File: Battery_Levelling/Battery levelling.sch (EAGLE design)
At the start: 36 parts, among them CON1 MOLEX_5566-2, CON2 SM03B-GHS-TB, CON3 SM03B-GHS-TB, J1 MKDS_5/2-6,352, J2 MKDS_5/2-6,352, J3 MKDS_5/2-6,352, J4 MKDS_5/2-6,352, J5 MKDS_5/2-6,352, U1 TEENSY_3.1_BASIC_2, U3 TCAN1042HVDR

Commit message: Added channel, changed CAN transceiver, used NMOS
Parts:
- removed T2: (no value), transistor-neu-to92:-NPN-SOT223
- removed U$2: LM5050-2, AlbertaSat:LM5050-2
- removed U$7: PMOS-SO8, AlbertaSat:PMOS-SO8
- added C6: 10u, rcl:C-EUC0805
- added C7: 1.5uF, adafruit:C-USC0805
- added C8: 10uF, adafruit:C-USC1206
- added D1: (no value), diode:DIODE-DO-214AC
- added J6: MKDS_5/2-6,352, Moira:MKDS_5/2-6,352
- added Q4: NMOS-TO252, AlbertaSat:NMOS-TO252
- added Q5: DMN2011UTS, Lydia:DMN2011UTS
- added R11: 100k, adafruit:R-US_R1206
- added U5: LM5050-2, AlbertaSat:LM5050-2
- added U6: IR2301S, Lydia:IR2301S
- added U7: MCP2562-E/SN, Lydia:MCP2562-E/SN
- C4: value 10u -> 0.01uF; device rcl:C-EUC0805 -> adafruit:C-USC0805
- R10: value 100k -> 1k; device adafruit:R-US_R1206 -> rcl:R-US_R0805
- R4: value 5k -> 5.1
- U3: value TCAN1042HVDR -> LM5050-2; device ARVP:TCAN1042HVDR -> AlbertaSat:LM5050-2
- renumbered U$1 to U2, U$3 to U4, U$4 to Q2, U$5 to Q1, U$6 to Q3
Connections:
- removed net VBATT0: R4.1, T2.C, U$7.G
- removed net VOUT1: J5.KL, U$2.OUT, U$7.D, U2.OUT, U4.OUT
- new net GATE4: Q4.G, U5.GATE
- new net GATE5: R10.1, U6.HO
- new net IO6: R11.1, U1.10/TX2/PWM, U5.NFGD
- new net N$4: C7.2, U6.VS
- new net N$5: C7.1, D1.C, U6.VB
- new net N$6: U7.VIO
- new net N$7: Q5.G, R10.2
- new net VBATT4: J6.KL1, Q4.S
- net +3V3: now also C6.1; no longer C4.1, U3.VIO
- net +5V: now also R11.2
- net CANH1: now also U7.CANH; no longer U3.CANH
- net CANL1: now also U7.CANL; no longer U3.CANL
- net CAN_RX1: now also U7.RXD; no longer U3.RXD
- net CAN_TX2: now also U7.TXD; no longer U3.TXD
- net GATE2: now also U3.GATE; no longer U$2.GATE
- net GND: now also C6.2, C8.2, J6.KL, U5.GND, U6.GND, U6.LIN, U7.VSS; no longer T2.E, U$2.GND
- net IO1: now also U6.HIN; no longer R10.2
- net IO2: now also U3.OFF, U5.OFF; no longer U$2.OFF
- net IO3: now also U3.NFGD; no longer U$2.NFGD
- net N$1: now also C8.1, Q5.D, R4.1, U6.VCC; no longer R4.2, U$7.S
- net N$3: now also D1.A, R4.2; no longer R10.1, T2.B
- net STB1: now also U7.STBY; no longer U3.STB
- net VBATT2: now also U3.IN; no longer U$2.IN
- net VBATT3: now also C4.1, U5.IN
- net VIN: now also U7.VDD; no longer U3.VCC
- net VOUT: now also J5.KL, Q4.D, Q5.S, U2.OUT, U3.OUT, U4.OUT, U5.OUT
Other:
- note added: "A high side NMOS switch controls the original electronics battery (BATT0) using a high side gate driver with a bootstap circuit. When the GPIO pin is low, the NMOS is not conducting. When the GPIO pin is high, the gate driver will turn on and drive the NMOS with battery voltage+bootstrap voltage."
- note added: "The bootstrap circuit uses a capacitor C7 to store charge on a low cycle. Stored charge will be used to bias VCC to increase the voltage at HO during high cycles in order to increase the voltage between the NMOS gate and source. C7 will slowly discharge during a high cycle, so the capcitance is chosen to be 10 times greater than the gate capacitance of the NMOS to prolong the discharge. The bypas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"
- note removed: "A PMOS controls the original electronics battery (BATT0) using a BJT and a GPIO pin. When the GPIO pin is low, the PMOS is not conducting. When the GPIO pin is high, current will flow through the transistor and the gate and source of the PMOS will have a voltage difference (Vg < Vs) causing the PMOSto conduct."
- note removed: "The BJT base current is designed to be 23uA. The BJT has a current gain of 25 at the design condition, giving a collector current of 0.58 mA. When the BJT is on, Vgs will be around -2.9V. The PMOS chosen has a Vth of -1.4V and will be turned on as well."
- moved on the sheet: C4, C5, CON2-1, CON2-2, CON2-3, CON2-TABS, CON3-1, CON3-2, CON3-3, CON3-TABS, R1, R10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

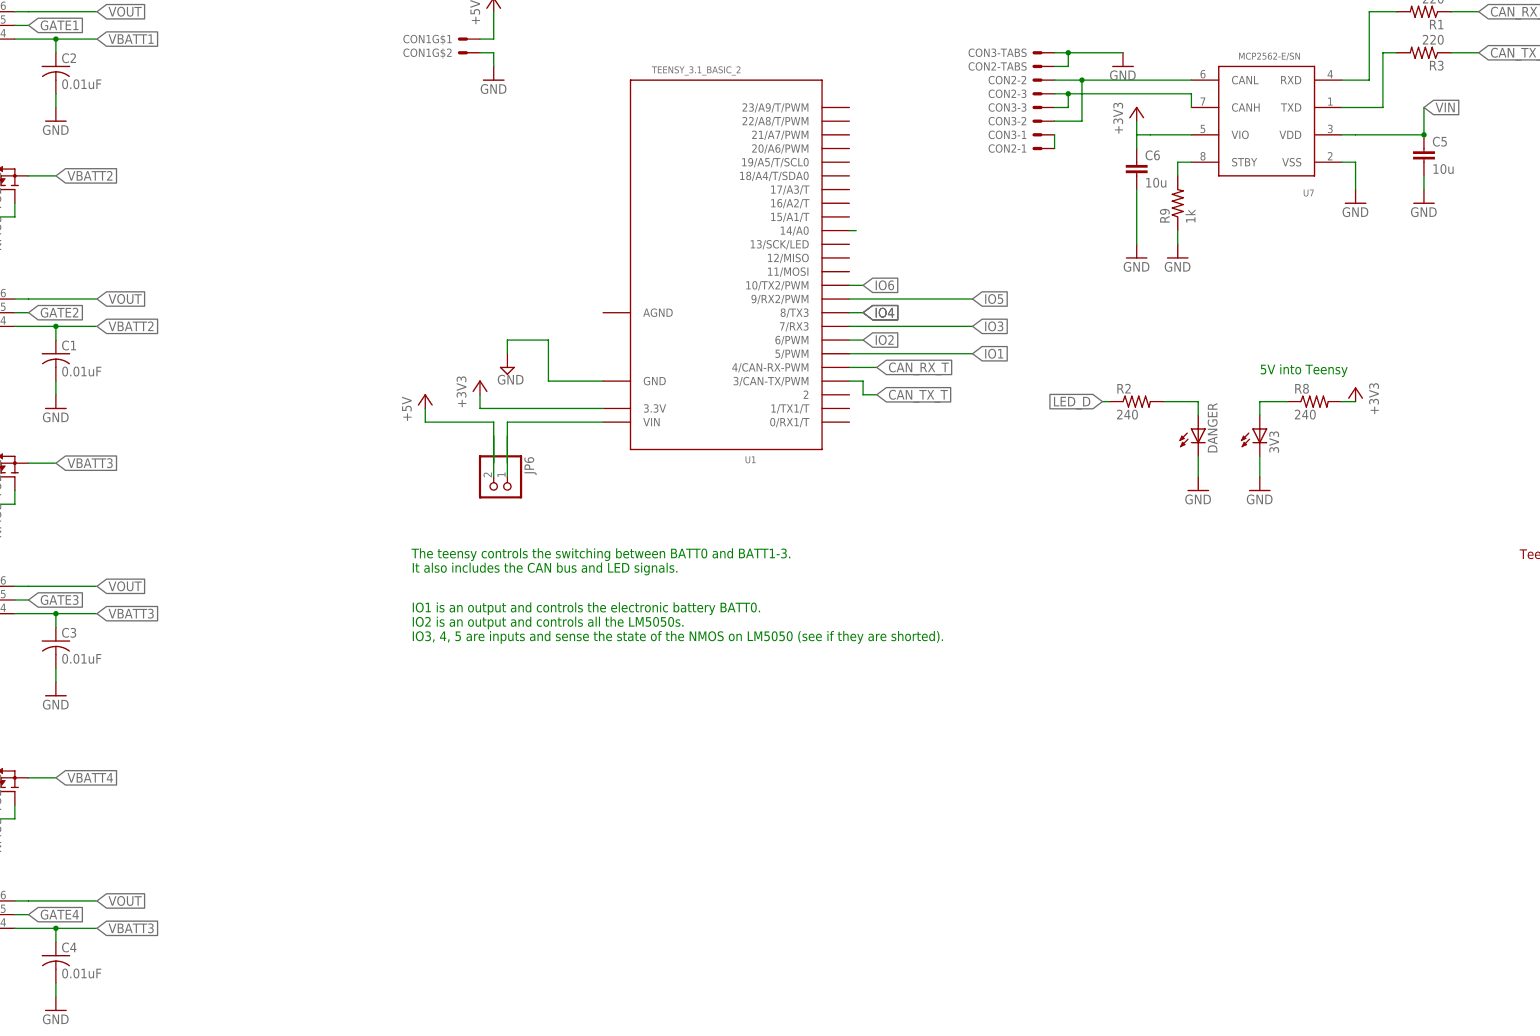
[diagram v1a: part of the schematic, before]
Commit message: Added PCB board file for battery levelling board
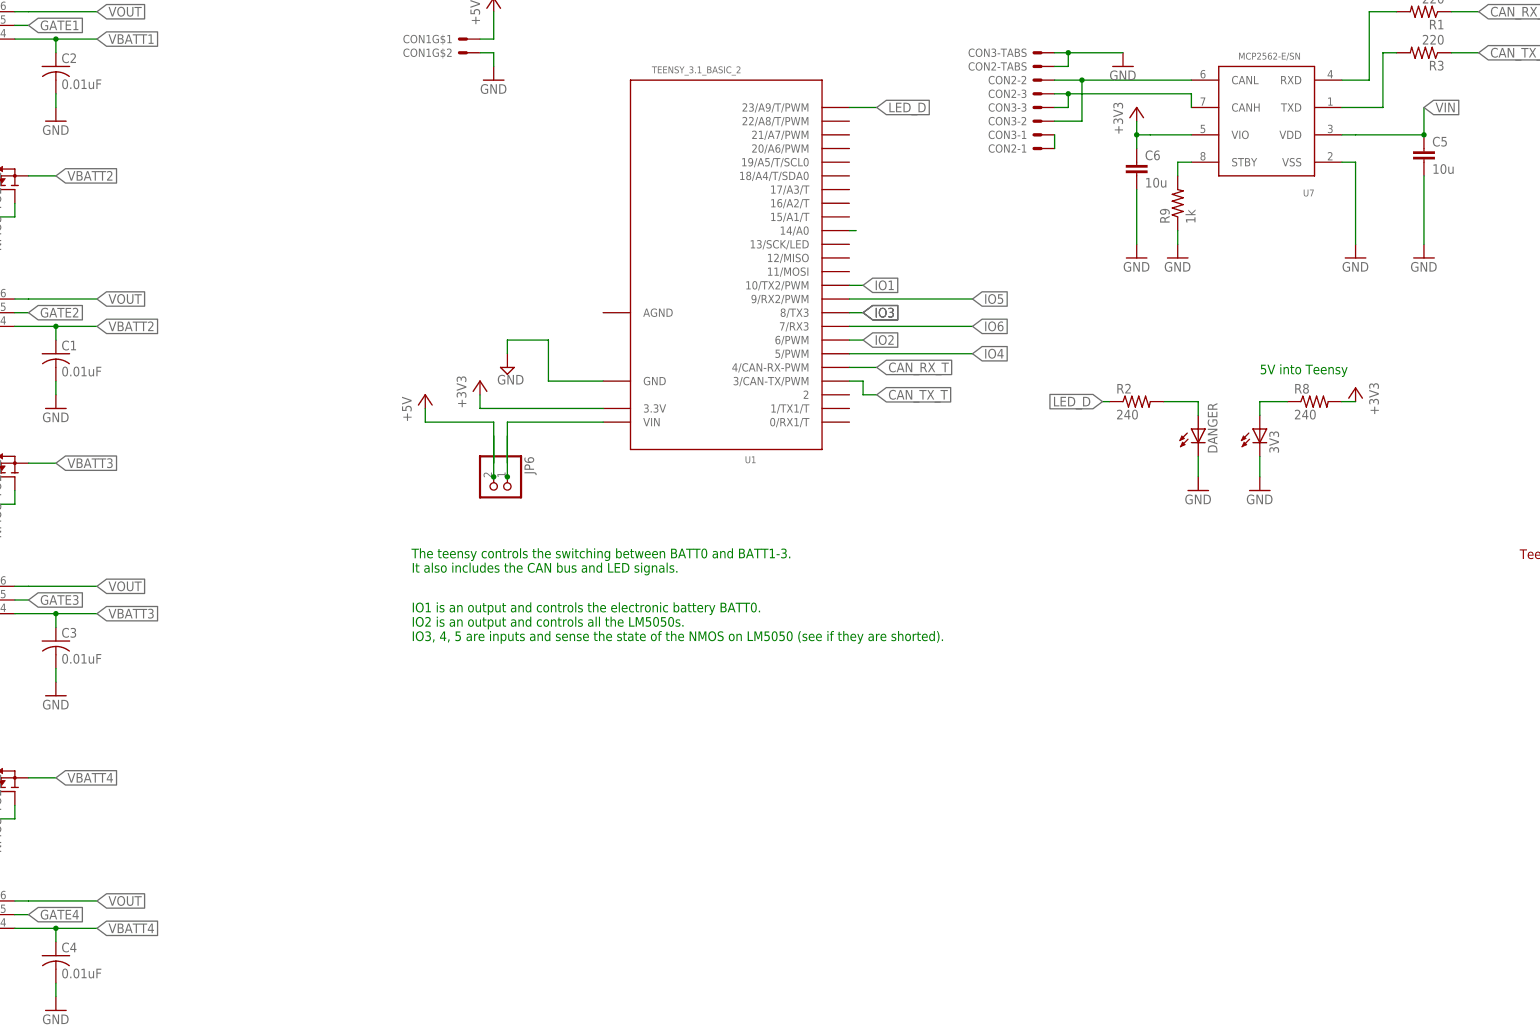
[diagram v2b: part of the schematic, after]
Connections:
- removed net N$6: U7.VIO
- net +3V3: now also U7.VIO
- net IO1: now also U1.10/TX2/PWM; no longer U1.5/PWM
- net IO3: now also U1.8/TX3; no longer U1.7/RX3
- net IO4: now also U1.5/PWM; no longer U1.8/TX3
- net IO6: now also U1.7/RX3; no longer U1.10/TX2/PWM
- net LED_D: now also U1.23/A9/T/PWM
- net VBATT3: no longer C4.1, U5.IN
- net VBATT4: now also C4.1, U5.IN
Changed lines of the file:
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@@
 <instance part="P+1" gate="1" x="152.4" y="-7.62"/>
 <instance part="+3V34" gate="G$1" x="284.48" y="45.72"/>
-<instance part="GND6" gate="1" x="325.12" y="27.94"/>
+<instance part="GND6" gate="1" x="325.12" y="17.78"/>
 <instance part="C6" gate="G$1" x="284.48" y="35.56"/>
 <instance part="GND7" gate="1" x="284.48" y="17.78"/>
 <instance part="C5" gate="G$1" x="337.82" y="38.1"/>
-<instance part="GND10" gate="1" x="337.82" y="27.94"/>
+<instance part="GND10" gate="1" x="337.82" y="17.78"/>
 <instance part="R9" gate="G$1" x="292.1" y="27.94" rot="R90"/>
 <instance part="GND11" gate="1" x="292.1" y="17.78"/>
@@
 <net name="IO1" class="0">
 <segment>
-<pinref part="U1" gate="G$1" pin="5/PWM"/>
-<wire x1="231.14" y1="0" x2="254" y2="0" width="0.1524" layer="91"/>
-<label x="254" y="0" size="1.778" layer="95" xref="yes"/>
-</segment>
-<segment>
 <wire x1="-106.68" y1="33.02" x2="-114.3" y2="33.02" width="0.1524" layer="91"/>
 <label x="-114.3" y="33.02" size="1.778" layer="95" rot="R180" xref="yes"/>
 <pinref part="U6" gate="G$1" pin="HIN"/>
+</segment>
+<segment>
+<wire x1="231.14" y1="12.7" x2="233.68" y2="12.7" width="0.1524" layer="91"/>
+<label x="233.68" y="12.7" size="1.778" layer="95" xref="yes"/>
+<pinref part="U1" gate="G$1" pin="10/TX2/PWM"/>
 </segment>
 </net>
@@
 <pinref part="Q3" gate="G$1" pin="S"/>
 </segment>
-<segment>
-<wire x1="76.2" y1="-106.68" x2="83.82" y2="-106.68" width="0.1524" layer="91"/>
-<label x="91.44" y="-106.68" size="1.778" layer="95" xref="yes"/>
-<pinref part="U5" gate="G$1" pin="IN"/>
-<pinref part="C4" gate="G$1" pin="1"/>
-<wire x1="83.82" y1="-106.68" x2="91.44" y2="-106.68" width="0.1524" layer="91"/>
-<wire x1="83.82" y1="-106.68" x2="83.82" y2="-109.22" width="0.1524" layer="91"/>
-<junction x="83.82" y="-106.68"/>
-</segment>
 </net>
 <net name="GATE3" class="0">
@@
 <pinref part="GND6" gate="1" pin="GND"/>
 <wire x1="322.58" y1="35.56" x2="325.12" y2="35.56" width="0.1524" layer="91"/>
-<wire x1="325.12" y1="35.56" x2="325.12" y2="30.48" width="0.1524" layer="91"/>
+<wire x1="325.12" y1="35.56" x2="325.12" y2="20.32" width="0.1524" layer="91"/>
 <pinref part="U7" gate="G$1" pin="VSS"/>
 </segment>
@@
 <pinref part="C5" gate="G$1" pin="2"/>
 <pinref part="GND10" gate="1" pin="GND"/>
-<wire x1="337.82" y1="33.02" x2="337.82" y2="30.48" width="0.1524" layer="91"/>
+<wire x1="337.82" y1="33.02" x2="337.82" y2="20.32" width="0.1524" layer="91"/>
 </segment>
 <segment>
@@
 </segment>
 <segment>
-<pinref part="U1" gate="G$1" pin="8/TX3"/>
-<wire x1="231.14" y1="7.62" x2="233.68" y2="7.62" width="0.1524" layer="91"/>
-<label x="233.68" y="7.62" size="1.778" layer="95" xref="yes"/>
-<label x="233.68" y="7.62" size="1.778" layer="95" xref="yes"/>
+<pinref part="U1" gate="G$1" pin="5/PWM"/>
+<wire x1="231.14" y1="0" x2="254" y2="0" width="0.1524" layer="91"/>
+<label x="254" y="0" size="1.778" layer="95" xref="yes"/>
 </segment>
 </net>
@@
 </segment>
 <segment>
-<pinref part="U1" gate="G$1" pin="7/RX3"/>
-<wire x1="231.14" y1="5.08" x2="254" y2="5.08" width="0.1524" layer="91"/>
-<label x="254" y="5.08" size="1.778" layer="95" xref="yes"/>
+<pinref part="U1" gate="G$1" pin="8/TX3"/>
+<wire x1="231.14" y1="7.62" x2="233.68" y2="7.62" width="0.1524" layer="91"/>
+<label x="233.68" y="7.62" size="1.778" layer="95" xref="yes"/>
+<label x="233.68" y="7.62" size="1.778" layer="95" xref="yes"/>
 </segment>
 </net>
@@
 <pinref part="+3V34" gate="G$1" pin="+3V3"/>
 <pinref part="C6" gate="G$1" pin="1"/>
-<wire x1="284.48" y1="43.18" x2="284.48" y2="38.1" width="0.1524" layer="91"/>
+<wire x1="284.48" y1="43.18" x2="284.48" y2="40.64" width="0.1524" layer="91"/>
+<pinref part="U7" gate="G$1" pin="VIO"/>
+<wire x1="284.48" y1="40.64" x2="284.48" y2="38.1" width="0.1524" layer="91"/>
+<wire x1="294.64" y1="40.64" x2="287.02" y2="40.64" width="0.1524" layer="91"/>
+<wire x1="284.48" y1="40.64" x2="287.02" y2="40.64" width="0.1524" layer="91"/>
+<junction x="284.48" y="40.64"/>
 </segment>
 </net>
@@
 <wire x1="279.4" y1="-8.89" x2="278.13" y2="-8.89" width="0.1524" layer="91"/>
 <label x="278.13" y="-8.89" size="1.778" layer="95" rot="R180" xref="yes"/>
+</segment>
+<segment>
+<pinref part="U1" gate="G$1" pin="23/A9/T/PWM"/>
+<wire x1="231.14" y1="45.72" x2="236.22" y2="45.72" width="0.1524" layer="91"/>
+<label x="236.22" y="45.72" size="1.778" layer="95" xref="yes"/>
 </segment>
 </net>
@@
 <pinref part="JP6" gate="G$1" pin="2"/>
 <wire x1="165.1" y1="-15.24" x2="165.1" y2="-22.86" width="0.1524" layer="91"/>
+<junction x="165.1" y="-22.86"/>
 </segment>
 </net>
@@
 <pinref part="JP6" gate="G$1" pin="1"/>
 <wire x1="167.64" y1="-22.86" x2="167.64" y2="-15.24" width="0.1524" layer="91"/>
+<junction x="167.64" y="-22.86"/>
 </segment>
 </net>
@@
 <pinref part="J6" gate="G$1" pin="KL1"/>
 </segment>
+<segment>
+<wire x1="76.2" y1="-106.68" x2="83.82" y2="-106.68" width="0.1524" layer="91"/>
+<label x="91.44" y="-106.68" size="1.778" layer="95" xref="yes"/>
+<pinref part="U5" gate="G$1" pin="IN"/>
+<pinref part="C4" gate="G$1" pin="1"/>
+<wire x1="83.82" y1="-106.68" x2="91.44" y2="-106.68" width="0.1524" layer="91"/>
+<wire x1="83.82" y1="-106.68" x2="83.82" y2="-109.22" width="0.1524" layer="91"/>
+<junction x="83.82" y="-106.68"/>
+</segment>
 </net>
 <net name="GATE4" class="0">
@@
 </segment>
 <segment>
-<wire x1="231.14" y1="12.7" x2="233.68" y2="12.7" width="0.1524" layer="91"/>
-<label x="233.68" y="12.7" size="1.778" layer="95" xref="yes"/>
-<pinref part="U1" gate="G$1" pin="10/TX2/PWM"/>
+<pinref part="U1" gate="G$1" pin="7/RX3"/>
+<wire x1="231.14" y1="5.08" x2="254" y2="5.08" width="0.1524" layer="91"/>
+<label x="254" y="5.08" size="1.778" layer="95" xref="yes"/>
 </segment>
 </net>
@@
 </segment>
 </net>
-<net name="N$6" class="0">
-<segment>
-<pinref part="U7" gate="G$1" pin="VIO"/>
-<wire x1="294.64" y1="40.64" x2="287.02" y2="40.64" width="0.1524" layer="91"/>
-<wire x1="284.48" y1="40.64" x2="287.02" y2="40.64" width="0.1524" layer="91"/>
-</segment>
-</net>

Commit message: battery_levelling: changed to 4-pin CAN
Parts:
- CON2, CON3: value SM03B-GHS-TB -> SM04B-GHS-TB; device ARVP:SM03B-GHS-TB -> ARVP:SM04B-GHS-TB
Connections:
- net CANH1 renamed CANH
- net CANL1 renamed CANL
- removed net CANSH1: CON2-1.S, CON3-1.S
- new net +5V_CAN: CON2-4.S, CON3-4.S
- net GND: now also CON2-1.S, CON3-1.S
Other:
- moved on the sheet: CON2-1, CON2-TABS, CON3-1, CON3-2, CON3-3, CON3-TABS
